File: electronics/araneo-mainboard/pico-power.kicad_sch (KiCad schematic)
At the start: 12 parts, among them IC3 TPS54302DDCR

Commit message: electronics: assign footprints
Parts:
- C12, C13, C19: footprint (none) -> PCM_JLCPCB:C_0603
- C14, C15, C17: footprint (none) -> PCM_JLCPCB:C_0402
- C16, C18: footprint (none) -> PCM_JLCPCB:C_0805
- IC3: footprint SOT95P280X110-6N -> Custom:SOT95P280X110-6N
- L1: footprint (none) -> Custom:PA4302103NLT
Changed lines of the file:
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@@
 			)
 		)
-		(property "Footprint" ""
+		(property "Footprint" "PCM_JLCPCB:C_0805"
 			(at 197.8152 66.04 0)
 			(hide yes)
@@
 			)
 		)
-		(property "Footprint" "SOT95P280X110-6N"
+		(property "Footprint" "Custom:SOT95P280X110-6N"
 			(at 156.21 148.26 0)
 			(hide yes)
@@
 			)
 		)
-		(property "Footprint" ""
+		(property "Footprint" "PCM_JLCPCB:C_0603"
 			(at 84.7852 66.04 0)
 			(hide yes)
@@
 			)
 		)
-		(property "Footprint" ""
+		(property "Footprint" "PCM_JLCPCB:C_0402"
 			(at 106.3752 66.04 0)
 			(hide yes)
@@
 			)
 		)
-		(property "Footprint" ""
+		(property "Footprint" "PCM_JLCPCB:C_0402"
 			(at 172.72 52.3748 0)
 			(hide yes)
@@
 			)
 		)
-		(property "Footprint" ""
+		(property "Footprint" "PCM_JLCPCB:C_0805"
 			(at 185.1152 66.04 0)
 			(hide yes)
@@
 			)
 		)
-		(property "Footprint" ""
+		(property "Footprint" "PCM_JLCPCB:C_0603"
 			(at 225.0948 50.8 0)
 			(hide yes)
@@
 			)
 		)
-		(property "Footprint" ""
+		(property "Footprint" "Custom:PA4302103NLT"
 			(at 179.07 58.42 0)
 			(hide yes)
@@
 			)
 		)
-		(property "Footprint" ""
+		(property "Footprint" "PCM_JLCPCB:C_0603"
 			(at 94.9452 66.04 0)
 			(hide yes)
@@
 			)
 		)
-		(property "Footprint" ""
+		(property "Footprint" "PCM_JLCPCB:C_0402"
 			(at 188.2648 49.53 0)
 			(hide yes)

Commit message: complete layout, revision need
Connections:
- net VBAT renamed VBAT_FUSED
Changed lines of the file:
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@@
 			)
 		)
-		(property "Value" "VBAT"
-			(at 80.01 52.07 0)
+		(property "Value" "VBAT_FUSED"
+			(at 82.55 55.8799 0)
 			(show_name no)
 			(do_not_autoplace no)
@@
 					(size 1.27 1.27)
 				)
+				(justify left)
 			)
 		)

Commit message: electronics: update bom
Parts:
- L1: now left out of the parts list
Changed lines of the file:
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@@
 		(body_style 1)
 		(exclude_from_sim no)
-		(in_bom yes)
+		(in_bom no)
 		(on_board yes)
 		(in_pos_files yes)

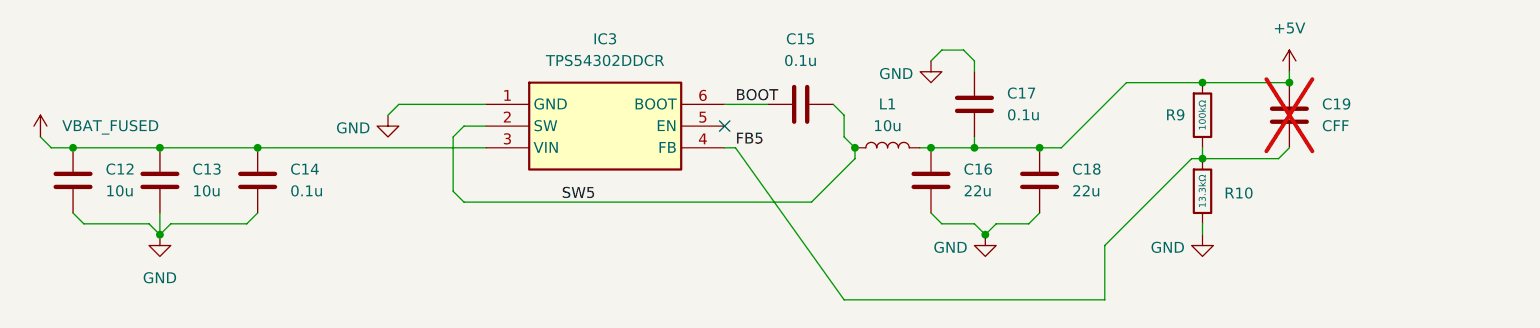
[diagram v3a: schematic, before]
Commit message: improve schematic and layout, add LCSC parts
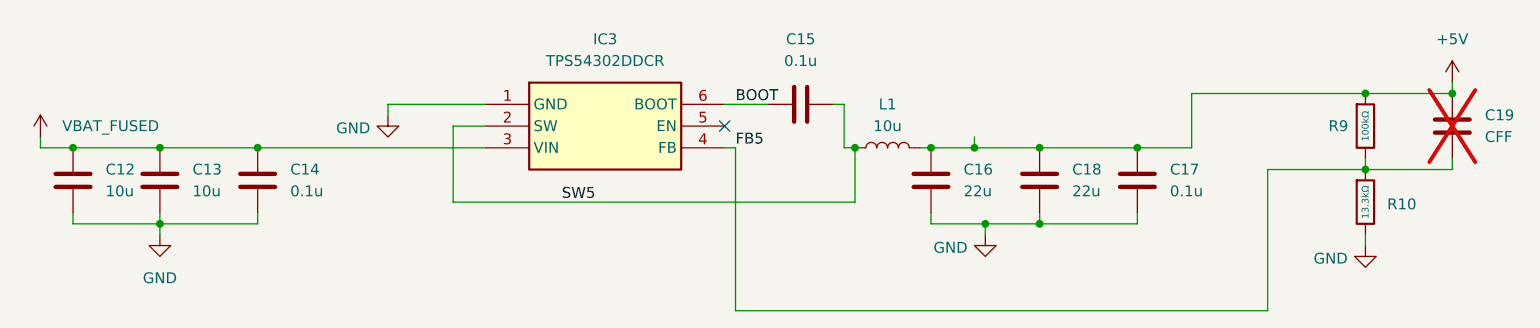
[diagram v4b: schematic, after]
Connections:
- net +5V: now also C17.2; no longer C17.1
- net GND: now also C17.1; no longer C17.2
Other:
- moved on the sheet: C19, R10, R9
